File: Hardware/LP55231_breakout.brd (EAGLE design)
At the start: 25.4 x 30.5 mm, 29 parts, among them J1 To micro, J2 USER LED, J3 USER LED, J4 USER LED, U1 LP55231WQFN

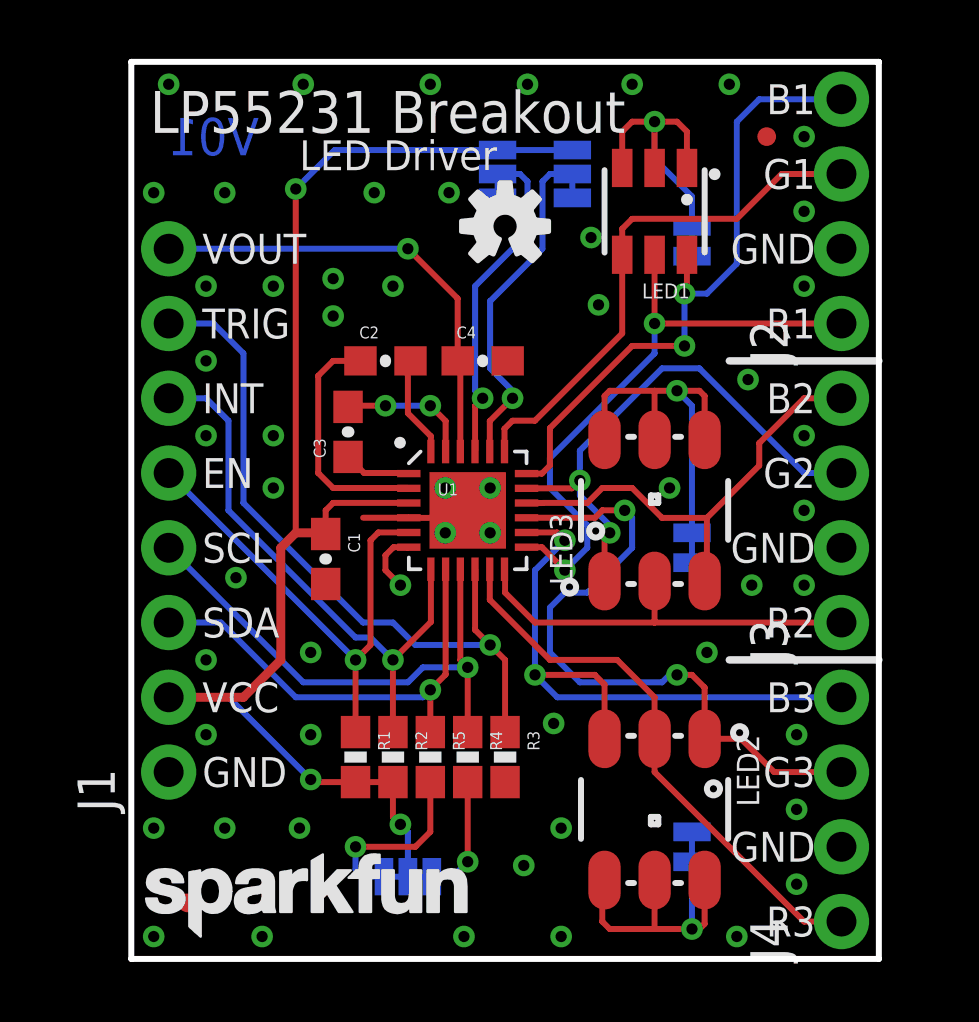
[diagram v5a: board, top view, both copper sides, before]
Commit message: Fixing review issues.
-Fiducial moved from under silk.
-Swapped numbering of LED's 2 & 3.
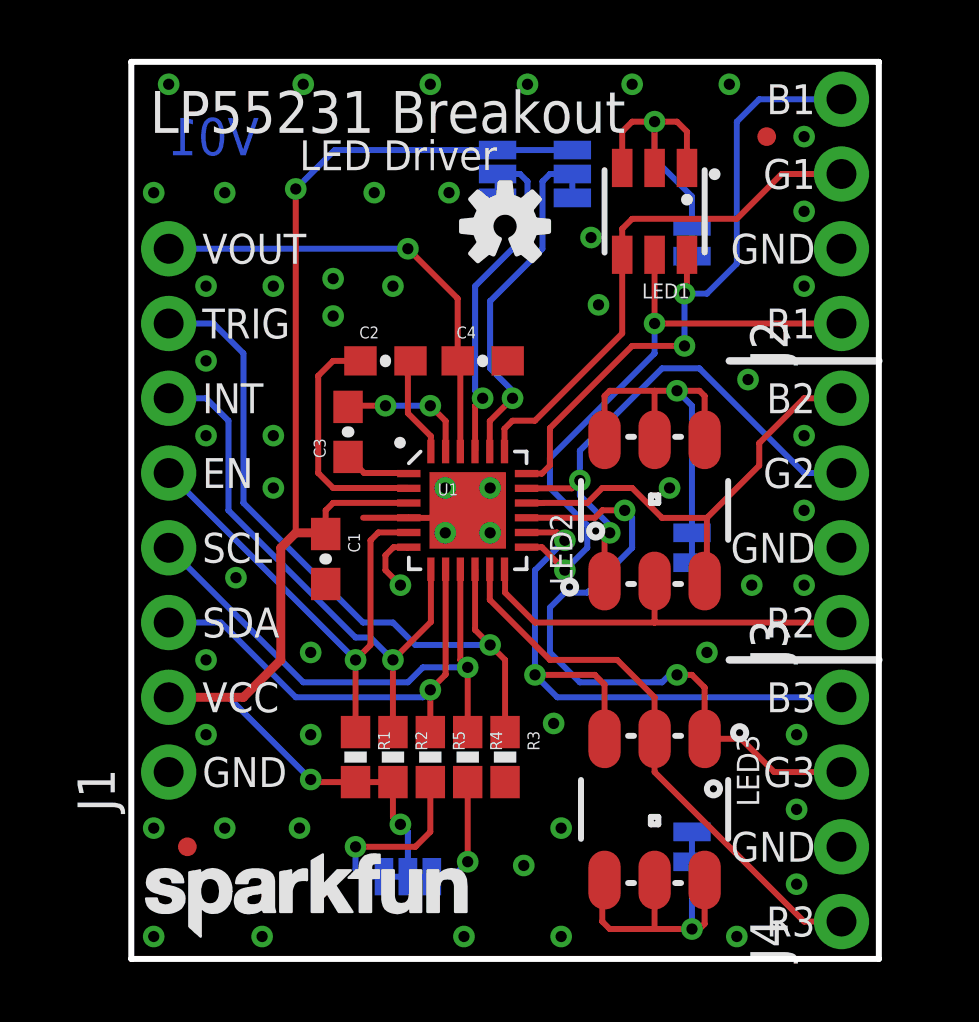
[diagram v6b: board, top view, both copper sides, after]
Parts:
- moved LED2 10.2 mm to (17.8, 15.2), turned to 90 degrees
- moved LED3 10.2 mm to (17.8, 5.08), turned to 270 degrees
- moved FD2 1.91 mm to (1.91, 3.81)
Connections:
- net B2: now also LED2.3; no longer LED3.3
- net B3: now also LED3.3; no longer LED2.3
- net G2: now also LED2.1; no longer LED3.1
- net G3: now also LED3.1; no longer LED2.1
- net N$1: now also LED3.4, LED3.5, LED3.6; no longer LED2.4, LED2.5, LED2.6
- net N$2: now also LED2.4, LED2.5, LED2.6; no longer LED3.4, LED3.5, LED3.6
- net R2: now also LED2.2; no longer LED3.2
- net R3: now also LED3.2; no longer LED2.2
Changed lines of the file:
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@@
 <setting verticaltext="up"/>
 </settings>
-<grid distance="0.01" unitdist="inch" unit="inch" style="lines" multiple="1" display="yes" altdistance="0.001" altunitdist="inch" altunit="inch"/>
+<grid distance="0.05" unitdist="inch" unit="inch" style="lines" multiple="1" display="yes" altdistance="0.005" altunitdist="inch" altunit="inch"/>
 <layers>
 <layer number="1" name="Top" color="4" fill="1" visible="yes" active="yes"/>
@@
 <layer number="49" name="Reference" color="7" fill="1" visible="no" active="yes"/>
 <layer number="50" name="dxf" color="7" fill="1" visible="no" active="no"/>
-<layer number="51" name="tDocu" color="6" fill="1" visible="no" active="yes"/>
+<layer number="51" name="tDocu" color="6" fill="1" visible="yes" active="yes"/>
 <layer number="52" name="bDocu" color="7" fill="1" visible="no" active="yes"/>
 <layer number="53" name="tGND_GNDA" color="7" fill="9" visible="no" active="no"/>
@@
 <element name="LOGO3" library="SparkFun-Aesthetics" package="OSHW-LOGO-S" value="OSHW-LOGOS" x="12.7" y="24.892"/>
 <element name="LOGO2" library="SparkFun-Aesthetics" package="SFE_LOGO_NAME_.1" value="SFE_LOGO_NAME.1_INCH" x="0" y="0.254"/>
-<element name="LED2" library="SparkFun-LED" package="LED-TRICOLOR-5050" value="TRICOLOR-5050" x="17.78" y="5.08" rot="R270">
+<element name="LED3" library="SparkFun-LED" package="LED-TRICOLOR-5050" value="TRICOLOR-5050" x="17.78" y="5.08" rot="R270">
 <attribute name="PROD_ID" value="DIO-10298" x="17.78" y="5.08" size="1.778" layer="27" rot="R270" display="off"/>
 </element>
@@
 <attribute name="PROD_ID" value="RES-07857" x="10.16" y="6.858" size="1.778" layer="27" font="vector" ratio="15" rot="R270" display="off"/>
 </element>
-<element name="FD2" library="SparkFun-Aesthetics" package="MICRO-FIDUCIAL" value="FIDUCIALUFIDUCIAL" x="1.905" y="1.905"/>
+<element name="FD2" library="SparkFun-Aesthetics" package="MICRO-FIDUCIAL" value="FIDUCIALUFIDUCIAL" x="1.905" y="3.81"/>
 <element name="FD1" library="SparkFun-Aesthetics" package="MICRO-FIDUCIAL" value="FIDUCIALUFIDUCIAL" x="21.59" y="27.94"/>
 <element name="JP4" library="SparkFun-Passives" package="PAD-JUMPER-2-NC_BY_TRACE_NO_SILK" value="Defeat LED1" x="19.05" y="24.384" rot="MR90"/>
@@
 </element>
 <element name="LOGO1" library="SparkFun-Aesthetics" package="SFE_LOGO_FLAME_.1" value="SFE_LOGO_FLAME.1_INCH" x="12.7" y="11.684" rot="MR0"/>
-<element name="LED3" library="SparkFun-LED" package="LED-TRICOLOR-5050" value="TRICOLOR-5050" x="17.78" y="15.24" rot="R90">
+<element name="LED2" library="SparkFun-LED" package="LED-TRICOLOR-5050" value="TRICOLOR-5050" x="17.78" y="15.24" rot="R90">
 <attribute name="PROD_ID" value="DIO-10298" x="17.78" y="15.24" size="1.778" layer="27" rot="R90" display="off"/>
 </element>
@@
 <signal name="R3">
 <contactref element="U1" pad="11"/>
-<contactref element="LED2" pad="2"/>
+<contactref element="LED3" pad="2"/>
 <contactref element="J4" pad="1"/>
 <wire x1="12.18" y1="12.204" x2="14.224" y2="10.16" width="0.2032" layer="1"/>
@@
 <signal name="G3">
 <contactref element="U1" pad="15"/>
-<contactref element="LED2" pad="1"/>
+<contactref element="LED3" pad="1"/>
 <contactref element="J4" pad="3"/>
 <via x="18.542" y="9.652" extent="1-16" drill="0.381"/>
@@
 <signal name="B3">
 <contactref element="U1" pad="14"/>
-<contactref element="LED2" pad="3"/>
+<contactref element="LED3" pad="3"/>
 <contactref element="J4" pad="4"/>
 <via x="14.732" y="14.224" extent="1-16" drill="0.381"/>
@@
 <wire x1="18.034" y1="14.986" x2="19.558" y2="14.986" width="0.2032" layer="1"/>
 <wire x1="13.43" y1="15.49" x2="13.966" y2="15.49" width="0.2032" layer="1"/>
-<contactref element="LED3" pad="3"/>
+<contactref element="LED2" pad="3"/>
 <wire x1="22.86" y1="19.05" x2="21.336" y2="17.526" width="0.2032" layer="1"/>
 <wire x1="21.336" y1="17.526" x2="21.336" y2="16.764" width="0.2032" layer="1"/>
@@
 <wire x1="13.716" y1="11.43" x2="17.78" y2="11.43" width="0.2032" layer="1"/>
 <wire x1="24.13" y1="11.43" x2="17.78" y2="11.43" width="0.2032" layer="1"/>
-<contactref element="LED3" pad="2"/>
+<contactref element="LED2" pad="2"/>
 <wire x1="17.78" y1="12.84" x2="17.78" y2="11.43" width="0.2032" layer="1"/>
 </signal>
@@
 <wire x1="18.034" y1="20.066" x2="15.24" y2="17.272" width="0.2032" layer="16"/>
 <wire x1="15.24" y1="17.272" x2="15.24" y2="16.256" width="0.2032" layer="16"/>
-<contactref element="LED3" pad="1"/>
+<contactref element="LED2" pad="1"/>
 <wire x1="16.08" y1="12.84" x2="16.08" y2="14.302" width="0.2032" layer="1"/>
 <via x="16.256" y="14.478" extent="1-16" drill="0.381"/>
@@
 </signal>
 <signal name="N$1">
-<contactref element="LED2" pad="4"/>
-<contactref element="LED2" pad="5"/>
-<contactref element="LED2" pad="6"/>
+<contactref element="LED3" pad="4"/>
+<contactref element="LED3" pad="5"/>
+<contactref element="LED3" pad="6"/>
 <contactref element="JP6" pad="2"/>
 <wire x1="19.48" y1="2.68" x2="19.48" y2="1.192" width="0.2032" layer="1"/>
@@
 <wire x1="19.05" y1="18.796" x2="18.542" y2="19.304" width="0.2032" layer="16"/>
 <via x="18.542" y="19.304" extent="1-16" drill="0.381"/>
-<contactref element="LED3" pad="4"/>
-<contactref element="LED3" pad="6"/>
-<contactref element="LED3" pad="5"/>
+<contactref element="LED2" pad="4"/>
+<contactref element="LED2" pad="6"/>
+<contactref element="LED2" pad="5"/>
 <wire x1="19.48" y1="17.64" x2="19.48" y2="19.128" width="0.2032" layer="1"/>
 <wire x1="19.48" y1="19.128" x2="19.304" y2="19.304" width="0.2032" layer="1"/>

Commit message: Updates to PCB after testing.
Preparing for second round of prototypes.
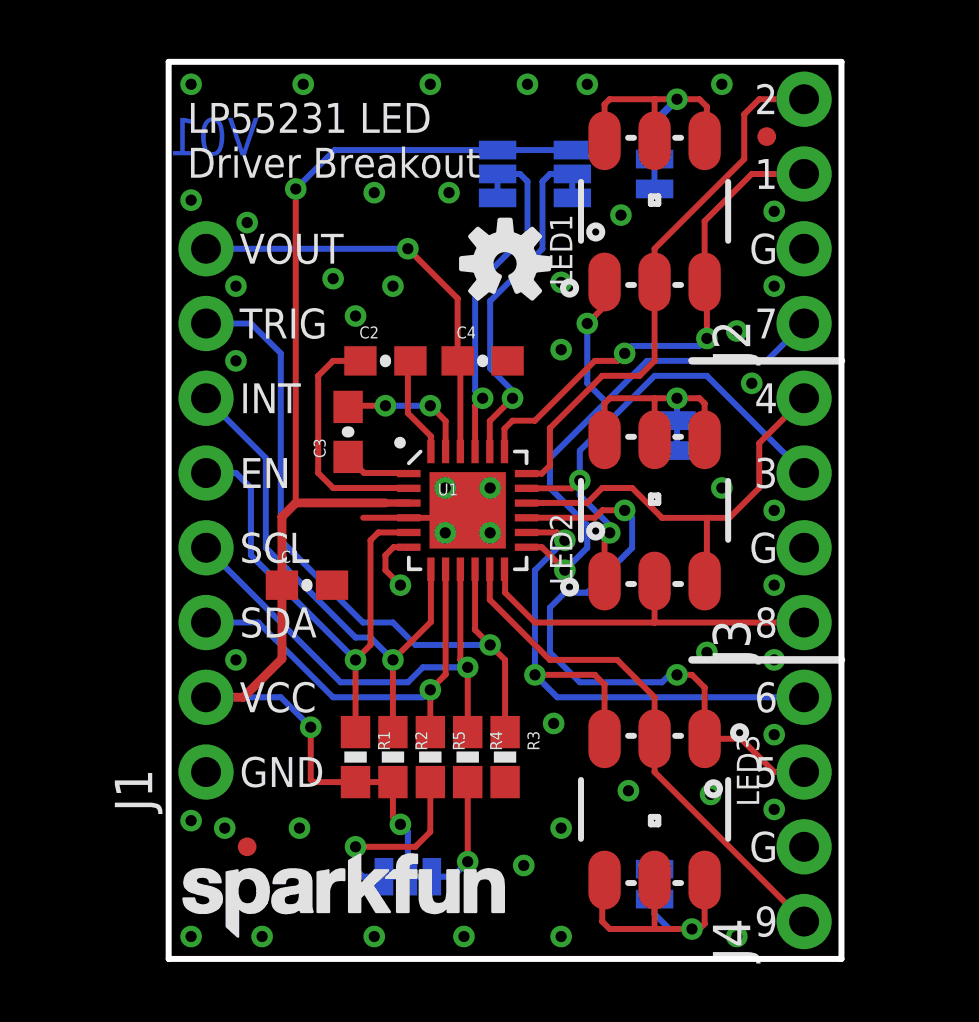
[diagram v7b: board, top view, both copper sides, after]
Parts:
- LED1: value TRICOLOR-PLCC-6 -> TRICOLOR-5050; device SparkFun-LED:PLCC-6-LED -> SparkFun-LED:LED-TRICOLOR-5050
- moved JP5 3.84 mm to (18.5, 17.8)
- moved JP4 2.62 mm to (17.8, 26.7)
- moved FD2 2.03 mm to (3.94, 3.81)
- moved JP6 1.80 mm to (17.8, 2.54)
- moved J1 1.27 mm to (2.54, 6.35)
- moved LOGO2 1.27 mm to (1.27, 0.25)
- moved J2 1.27 mm to (22.9, 21.6)
- moved J3 1.27 mm to (22.9, 11.4)
- moved J4 1.27 mm to (22.9, 1.27)
- moved LOGO3 1.27 mm to (12.7, 23.6)
- moved C1 1.09 mm to (5.97, 12.7), turned to 0 degrees
- turned LED1 to 90 degrees
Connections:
- net B1: now also LED1.2; no longer LED1.AB
- net G1: now also LED1.3; no longer LED1.AG
- net N$3: now also LED1.4, LED1.5, LED1.6; no longer LED1.CB, LED1.CG, LED1.CR
- net R1: now also LED1.1; no longer LED1.AR
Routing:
- net N$2: track 13.2 -> 8.19 mm
- net B1: track 21.9 -> 18.6 mm, vias 2 -> 0
- net VCC: track 47.5 -> 45.1 mm
- net G2: track 18.4 -> 16.9 mm
- net SCL: track 17.9 -> 16.6 mm
- net G3: track 22.8 -> 21.5 mm
- net B3: track 21.5 -> 20.2 mm
- net SDA: track 15.8 -> 14.5 mm
- net VOUT: track 15.8 -> 14.5 mm
- net R3: track 19.0 -> 17.7 mm
- net R2: track 14.1 -> 12.8 mm
- net INT: track 19.2 -> 17.9 mm
- net G1: track 17.9 -> 17.0 mm, vias 0 -> 2
- net B2: track 15.6 -> 14.8 mm
- net N$3: track 10.6 -> 9.84 mm
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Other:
- board size 25.4 x 30.5 mm -> 22.9 x 30.5 mm
- board text added: "1"
- board text added: "2"
- board text added: "3"
- board text added: "4"
- board text added: "5"
- board text added: "6"
- board text added: "7"
- board text added: "8"
- board text added: "9"
- board text added: "D2"
- board text added: "G"
- board text added: "LP55231 LED Driver Breakout"
- board text removed: "LED Driver"
- board text removed: "LP55231 Breakout"

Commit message: Updates after group review.
Addressing things in issue #3:
-bump version number
-Add silk indicating flooded/empty configuration on A0/A1
-space out passives on front (check tkeepout)
-remove extra junction dot between 150k res and Vcc on schematic
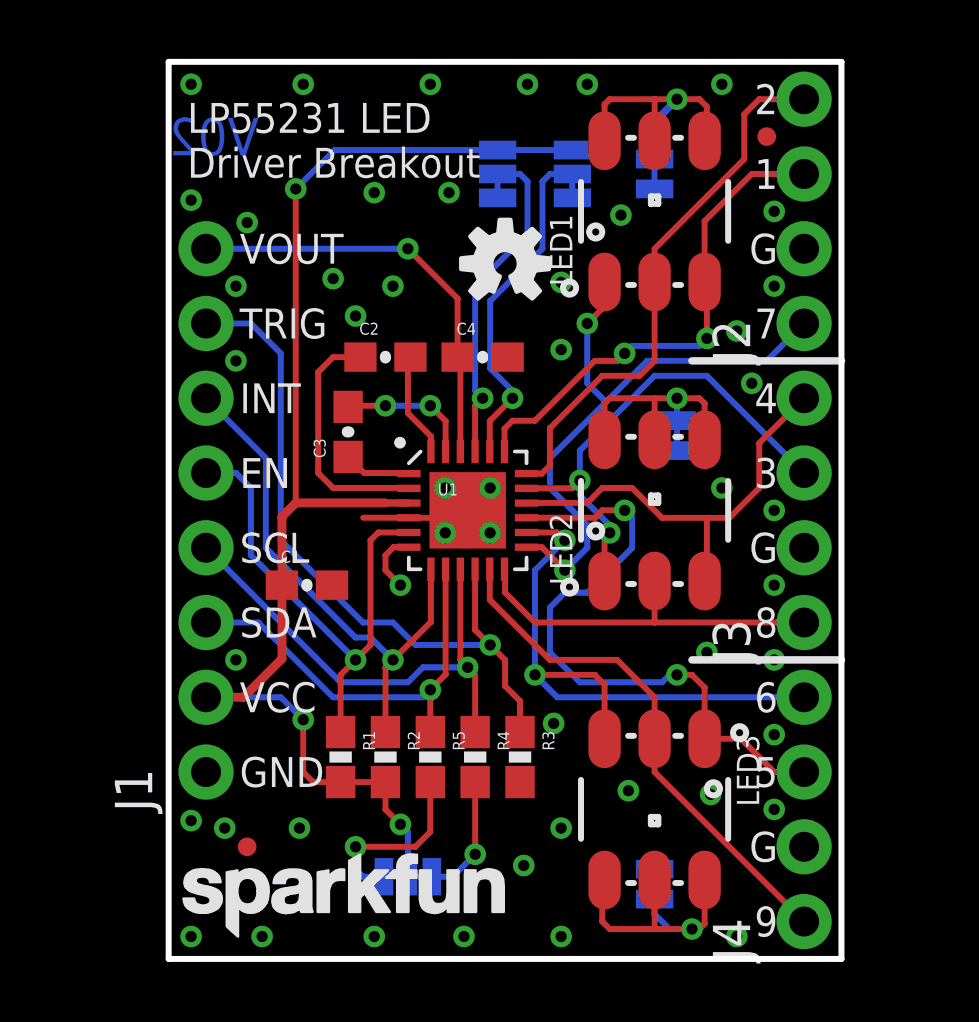
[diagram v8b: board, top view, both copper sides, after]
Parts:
- moved LOGO1 16.5 mm to (4.70, 26.2)
- moved R3 0.51 mm to (13.2, 6.86)
- moved R1 0.51 mm to (7.11, 6.86)
- moved R2 0.25 mm to (8.64, 6.86)
- moved R4 0.25 mm to (11.7, 6.86)
- moved C2 0.13 mm to (8.64, 20.4)
- moved C4 0.13 mm to (11.9, 20.4)
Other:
- board text added: "No!"
- board text added: "V02"
- board text added: "or"
- board text removed: "V01"
